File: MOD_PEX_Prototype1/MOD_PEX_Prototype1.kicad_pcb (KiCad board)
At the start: 2 copper layers, 78.4 x 40 mm, 72 parts, among them CN1 CONN_PANNEL_2X2, CN2 CONN_PANNEL_2X2, J1 RJ45_CHAIN_MAIN, J2 RJ45_CHAIN_EXTENSION, P1 HEADER_3X1, P2 HEADER_5X2, P3 HEADER_5X2, P4 HEADER_2X1, Q1 MMBT3904, Q2 MMBT3906, SW1 SWITCH_HH, U1 LPC111X_LQFP48, U2 AP1117E50G, U3 AP1117E33G, U4 MAX13450E, X1 10MHz

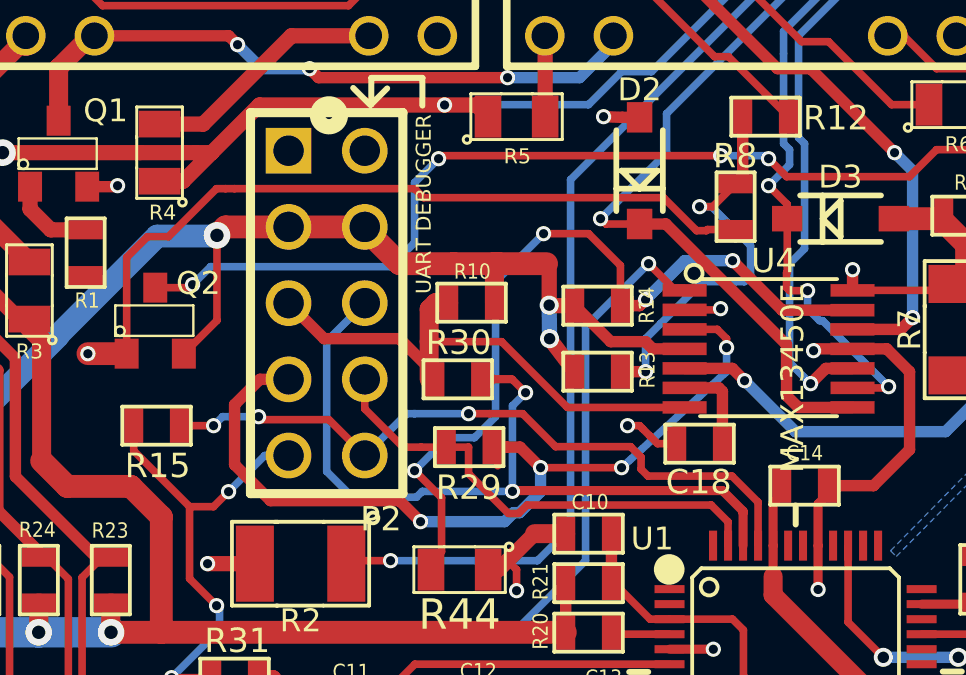
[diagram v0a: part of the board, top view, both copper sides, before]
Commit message: fix issue #12: Use 3.3V for Lv in the control chain circuit (updated the pcb layout and regenerated gerber files)
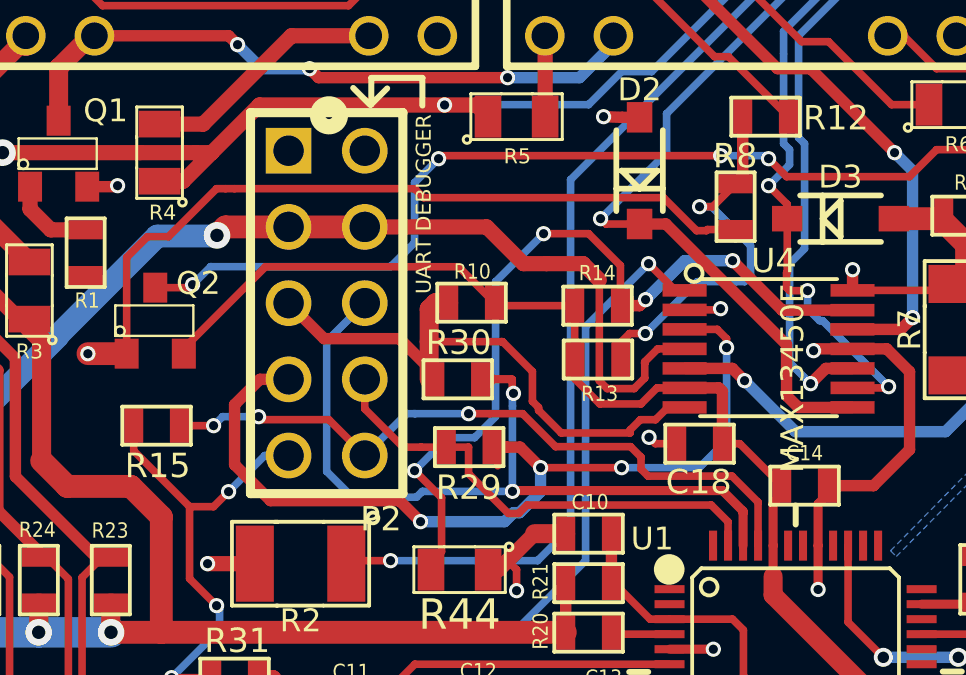
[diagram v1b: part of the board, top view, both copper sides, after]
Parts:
- R12: value 10k -> 100k
- moved R13 0.41 mm to (115.1, 85.4)
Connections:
- C18 pad 1: Net-(C18-Pad1) -> +3.3V
- Q2 pad 2: +5V -> +3.3V
- R10 pad 1: +5V -> +3.3V
- R13 pad 1: +5V -> +3.3V
- R14 pad 1: +5V -> +3.3V
- U4 pad 6: Net-(C18-Pad1) -> +3.3V
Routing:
- net +3.3V: track 198.8 -> 225.9 mm
- net +5V: track 43.3 -> 37.7 mm, vias 4 -> 2
- net Net-(C18-Pad1): track 3.05 -> 0.00 mm
- net TX_CHAIN: track 29.2 -> 30.6 mm
- net RX_CHAIN: track 18.5 -> 19.9 mm
- net DGND: track 173.1 -> 172.2 mm
- net Net-(R12-Pad2): track 13.6 -> 13.0 mm
